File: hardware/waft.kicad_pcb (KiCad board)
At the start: 2 copper layers, 58 x 109 mm, 57 parts, among them IC1 VL6180x_Composite, J1 CONN_01X02, J10 Conn_01x10_Female, J11 Conn_01x10_Male, J12 Conn_01x10_Male, J2 CONN_01X01, J3 Thonkiconn, J4 Conn_02x05_Odd_Even, J5 Thonkiconn, J6 Thonkiconn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

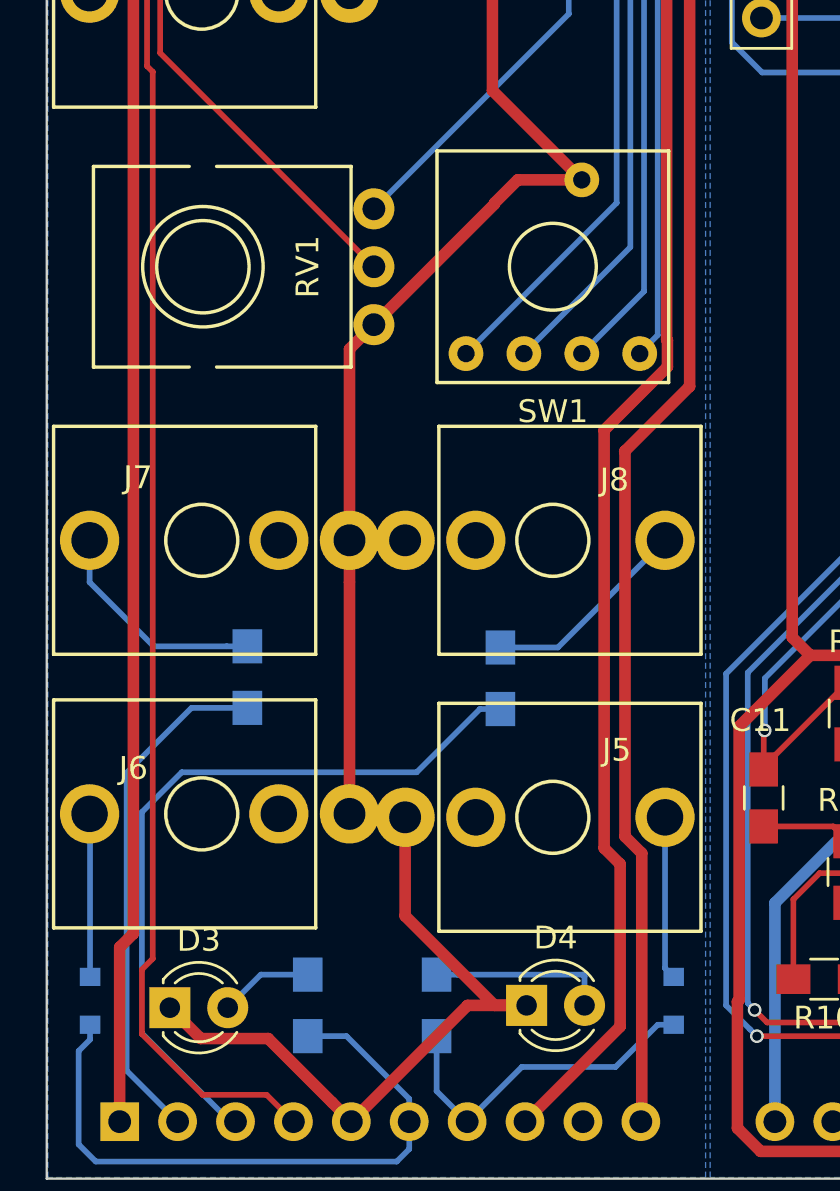
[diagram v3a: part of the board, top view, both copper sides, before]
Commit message: Started Front panel design
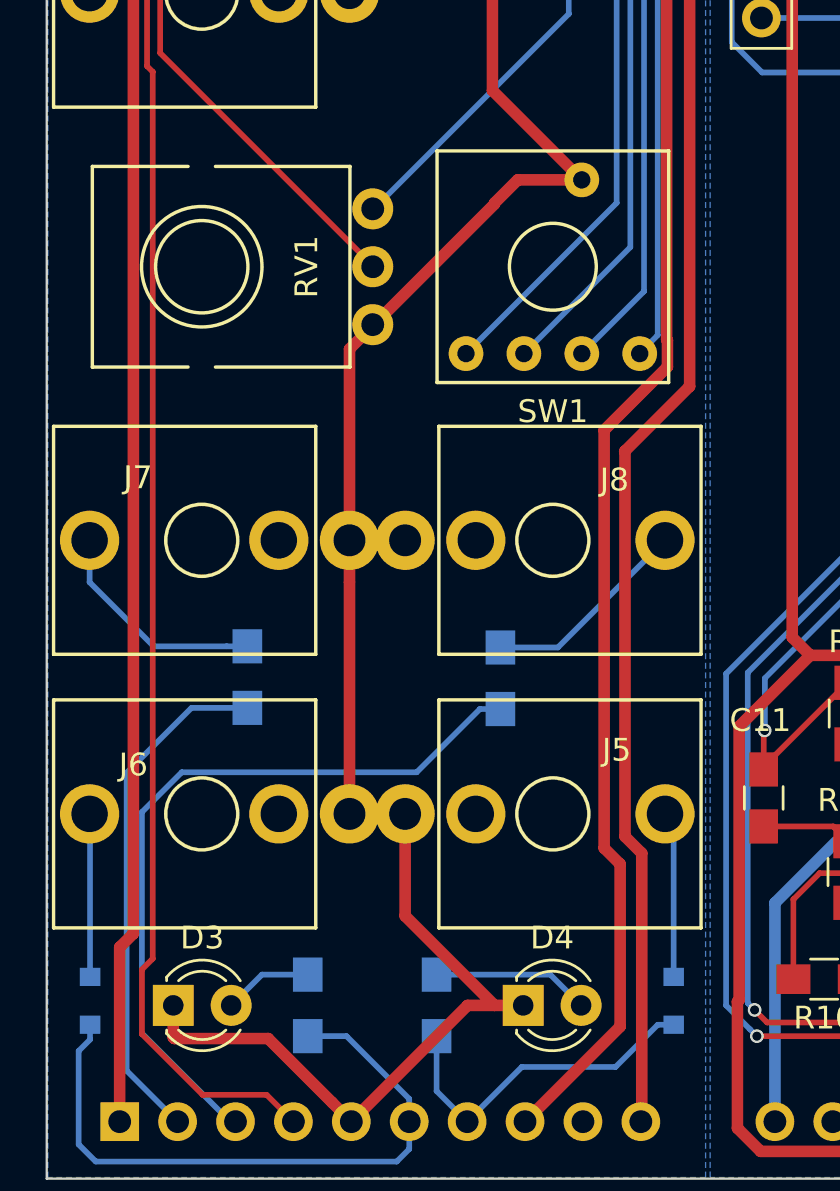
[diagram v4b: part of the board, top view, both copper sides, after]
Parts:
- moved D3 0.18 mm to (46.4, 152.8)
- moved J6 0.15 mm to (63.0, 144.4)
- moved D4 0.15 mm to (61.8, 152.8)
- moved RV1 0.05 mm to (47.6, 120.4)
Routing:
- net Net-(D4-Pad2): track 7.79 -> 6.90 mm
- net GND: track 446.9 -> 446.1 mm
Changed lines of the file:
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@@
   (general
     (links 148)
-    (no_connects 148)
-    (area 40.799999 51.349999 98.900001 160.450001)
+    (no_connects 5)
+    (area 39.015 46.104761 100.535 165.695239)
     (thickness 1.6)
     (drawings 12)
-    (tracks 651)
+    (tracks 649)
     (zones 0)
     (modules 57)
@@
   )
   (module LEDs:LED_D3.0mm (layer F.Cu)
-    (at 46.25 152.9)
+    (at 46.4 152.8)
     (descr "LED, diameter 3.0mm, 2 pins")
     (tags "LED diameter 3.0mm 2 pins")
@@
   )
   (module LEDs:LED_D3.0mm (layer F.Cu)
-    (at 61.9 152.8)
+    (at 61.75 152.8)
     (descr "LED, diameter 3.0mm, 2 pins")
     (tags "LED diameter 3.0mm 2 pins")
@@
   )
   (module europi:Thonkiconn (layer F.Cu)
-    (at 63.05 144.55 270)
+    (at 63.05 144.4 270)
     (fp_text reference J6 (at -2.15 18.4 360) (layer F.SilkS)
       (effects (font (size 1 1) (thickness 0.15)))
@@
   )
   (module europi:Alpha_9mm_Vertical (layer F.Cu)
-    (at 47.7 120.4 90)
+    (at 47.65 120.4 90)
     (fp_text reference RV1 (at 0 4.6 90) (layer F.SilkS)
       (effects (font (size 1 1) (thickness 0.15)))
@@
   (segment (start 73.05 53.9) (end 73.05 55.258) (width 0.508) (layer F.Cu) (net 1))
   (segment (start 73.05 55.258) (end 71.65 56.658) (width 0.508) (layer F.Cu) (net 1))
+  (segment (start 46.4 152.8) (end 46.4 154.208) (width 0.508) (layer F.Cu) (net 2))
+  (segment (start 46.4 154.208) (end 46.446001 154.254001) (width 0.508) (layer F.Cu) (net 2))
+  (segment (start 46.446001 154.254001) (end 50.564001 154.254001) (width 0.508) (layer F.Cu) (net 2))
+  (segment (start 50.564001 154.254001) (end 53.360001 157.050001) (width 0.508) (layer F.Cu) (net 2))
+  (segment (start 53.360001 157.050001) (end 54.21 157.9) (width 0.508) (layer F.Cu) (net 2))
+  (segment (start 60.492 152.8) (end 59.31 152.8) (width 0.508) (layer F.Cu) (net 2))
+  (segment (start 61.75 152.8) (end 60.492 152.8) (width 0.508) (layer F.Cu) (net 2))
+  (segment (start 56.57 148.878) (end 56.57 144.4) (width 0.508) (layer F.Cu) (net 2))
+  (segment (start 54.13 144.4) (end 56.57 144.4) (width 0.508) (layer F.Cu) (net 2))
   (segment (start 85.75 53.9) (end 85.75 57) (width 0.508) (layer F.Cu) (net 2))
   (segment (start 85.75 57) (end 86.59 57.84) (width 0.508) (layer F.Cu) (net 2))
@@
   (segment (start 78.53 96.64) (end 83.61 91.56) (width 0.508) (layer B.Cu) (net 2))
   (segment (start 83.61 91.56) (end 93.77 91.56) (width 0.508) (layer B.Cu) (net 2))
-  (segment (start 46.25 152.9) (end 47.604001 154.254001) (width 0.508) (layer F.Cu) (net 2))
-  (segment (start 47.604001 154.254001) (end 50.564001 154.254001) (width 0.508) (layer F.Cu) (net 2))
-  (segment (start 50.564001 154.254001) (end 53.360001 157.050001) (width 0.508) (layer F.Cu) (net 2))
-  (segment (start 53.360001 157.050001) (end 54.21 157.9) (width 0.508) (layer F.Cu) (net 2))
   (segment (start 54.21 157.9) (end 59.31 152.8) (width 0.508) (layer F.Cu) (net 2))
-  (segment (start 59.31 152.8) (end 61.9 152.8) (width 0.508) (layer F.Cu) (net 2))
-  (segment (start 56.57 144.55) (end 56.57 148.878) (width 0.508) (layer F.Cu) (net 2))
   (segment (start 56.57 148.878) (end 60.492 152.8) (width 0.508) (layer F.Cu) (net 2))
-  (segment (start 60.492 152.8) (end 61.9 152.8) (width 0.508) (layer F.Cu) (net 2))
-  (segment (start 54.13 144.4) (end 56.42 144.4) (width 0.508) (layer F.Cu) (net 2))
-  (segment (start 56.42 144.4) (end 56.57 144.55) (width 0.508) (layer F.Cu) (net 2))
   (segment (start 54.13 132.4) (end 54.13 134.238477) (width 0.508) (layer F.Cu) (net 2))
   (segment (start 54.13 134.238477) (end 54.13 144.4) (width 0.508) (layer F.Cu) (net 2))
@@
   (segment (start 97.05 67.392) (end 97.05 69) (width 0.508) (layer B.Cu) (net 17))
   (segment (start 89.13 60.73) (end 89.13 63.27) (width 0.508) (layer F.Cu) (net 17))
-  (segment (start 48.79 152.9) (end 50.24 151.45) (width 0.25) (layer B.Cu) (net 18))
-  (segment (start 50.24 151.45) (end 52.3 151.45) (width 0.25) (layer B.Cu) (net 18))
-  (segment (start 64.44 152.8) (end 64.44 151.527208) (width 0.25) (layer B.Cu) (net 19))
-  (segment (start 64.44 151.527208) (end 64.362792 151.45) (width 0.25) (layer B.Cu) (net 19))
-  (segment (start 64.362792 151.45) (end 58.85 151.45) (width 0.25) (layer B.Cu) (net 19))
-  (segment (start 58.85 151.45) (end 57.95 151.45) (width 0.25) (layer B.Cu) (net 19))
+  (segment (start 48.94 152.8) (end 50.29 151.45) (width 0.25) (layer B.Cu) (net 18))
+  (segment (start 50.29 151.45) (end 52.3 151.45) (width 0.25) (layer B.Cu) (net 18))
+  (segment (start 57.95 151.45) (end 62.94 151.45) (width 0.25) (layer B.Cu) (net 19))
+  (segment (start 62.94 151.45) (end 64.29 152.8) (width 0.25) (layer B.Cu) (net 19))
   (segment (start 42.75 151.55) (end 42.75 144.42) (width 0.25) (layer B.Cu) (net 20))
   (segment (start 42.75 144.42) (end 42.73 144.4) (width 0.25) (layer B.Cu) (net 20))
-  (segment (start 67.97 144.55) (end 67.97 151.17) (width 0.25) (layer B.Cu) (net 21))
-  (segment (start 67.97 151.17) (end 68.35 151.55) (width 0.25) (layer B.Cu) (net 21))
+  (segment (start 68.35 151.55) (end 68.35 144.78) (width 0.25) (layer B.Cu) (net 21))
+  (segment (start 68.35 144.78) (end 67.97 144.4) (width 0.25) (layer B.Cu) (net 21))
   (segment (start 72.2 92.7) (end 72.2 99.1) (width 0.25) (layer F.Cu) (net 22))
   (segment (start 72.2 92.7) (end 72.2 86.5) (width 0.25) (layer F.Cu) (net 22))

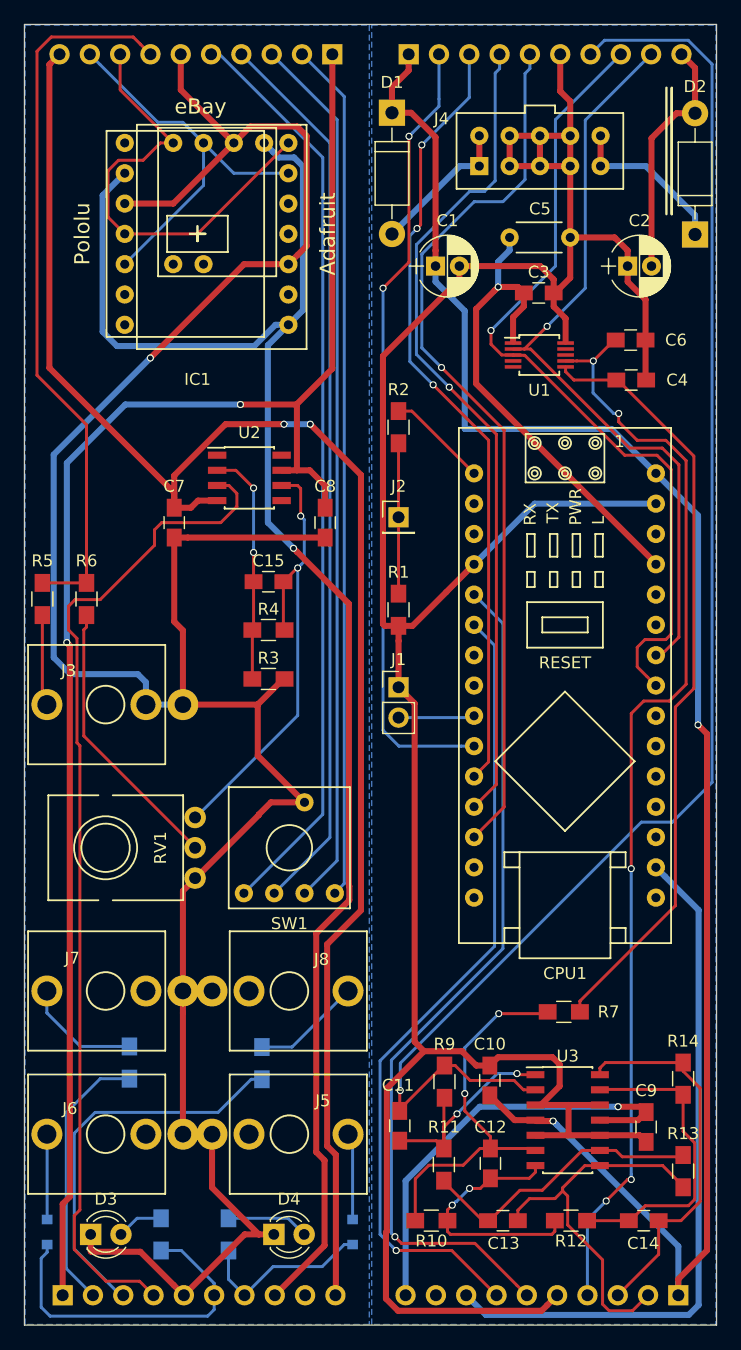
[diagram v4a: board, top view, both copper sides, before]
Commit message: Silk screen graphics
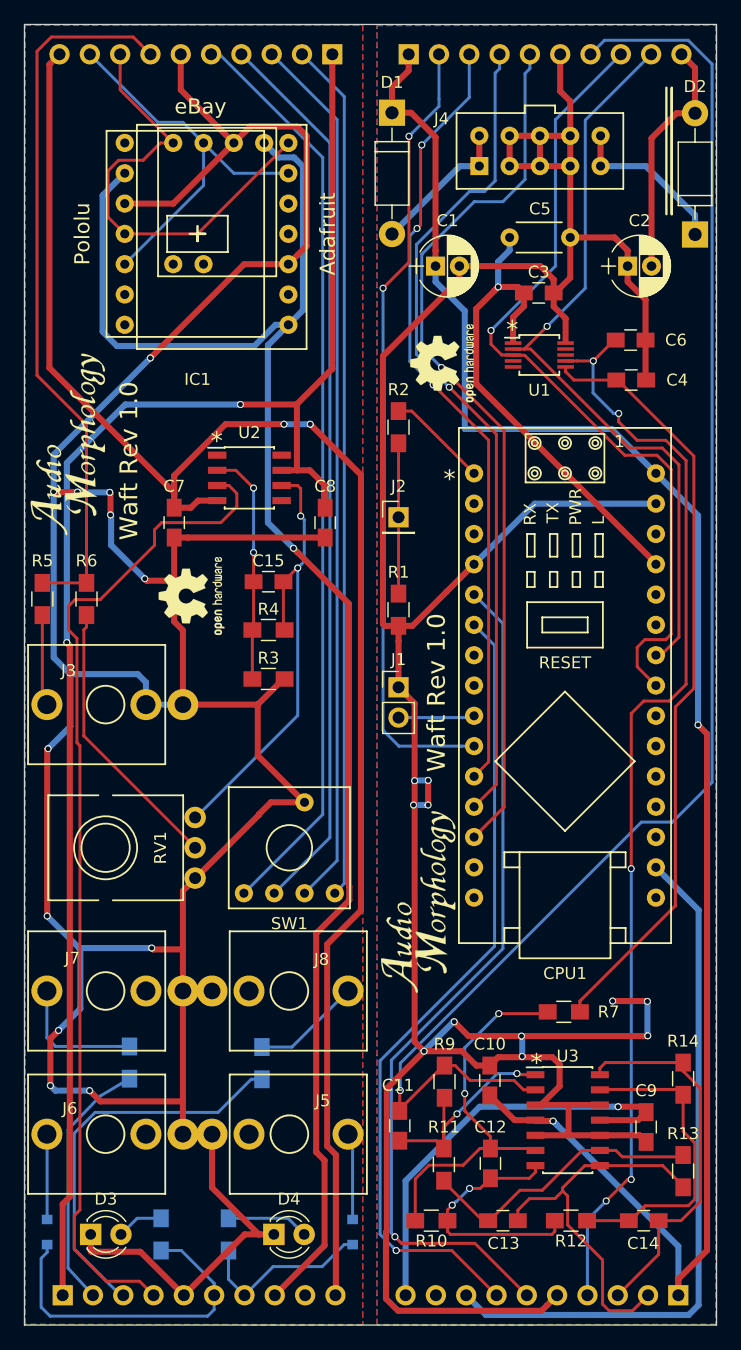
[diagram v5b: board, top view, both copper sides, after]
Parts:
- added ?: , europi:AM_Logo, F.Cu at (73.8, 125.0)
- added ?: , europi:AM_Logo, B.Cu at (86.6, 98.1)
- added ?: , europi:AM_Logo, F.Cu at (44.5, 86.6)
- added ?: , europi:AM_Logo, B.Cu at (53.3, 89.3)
- added REF***: OSHW-Logo2_7.3x6mm_SilkScreen, Symbols:OSHW-Logo2_7.3x6mm_SilkScreen, F.Cu at (54.9, 99.3)
- added REF***: OSHW-Logo2_7.3x6mm_SilkScreen, Symbols:OSHW-Logo2_7.3x6mm_SilkScreen, F.Cu at (75.9, 79.8)
- added REF***: OSHW-Logo2_7.3x6mm_SilkScreen, Symbols:OSHW-Logo2_7.3x6mm_SilkScreen, B.Cu at (88.1, 132.0)
- added REF***: OSHW-Logo2_7.3x6mm_SilkScreen, Symbols:OSHW-Logo2_7.3x6mm_SilkScreen, B.Cu at (53.4, 100.0)
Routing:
- net GND: track 446.1 -> 552.5 mm, vias 1 -> 23
- net CV1b: track 22.7 -> 21.4 mm
- net Net-(J7-Pad3): track 9.92 -> 11.1 mm
- added copper zone on F.Cu, net GND
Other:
- board text added: "*"
- board text added: "Waft Rev 1.0"

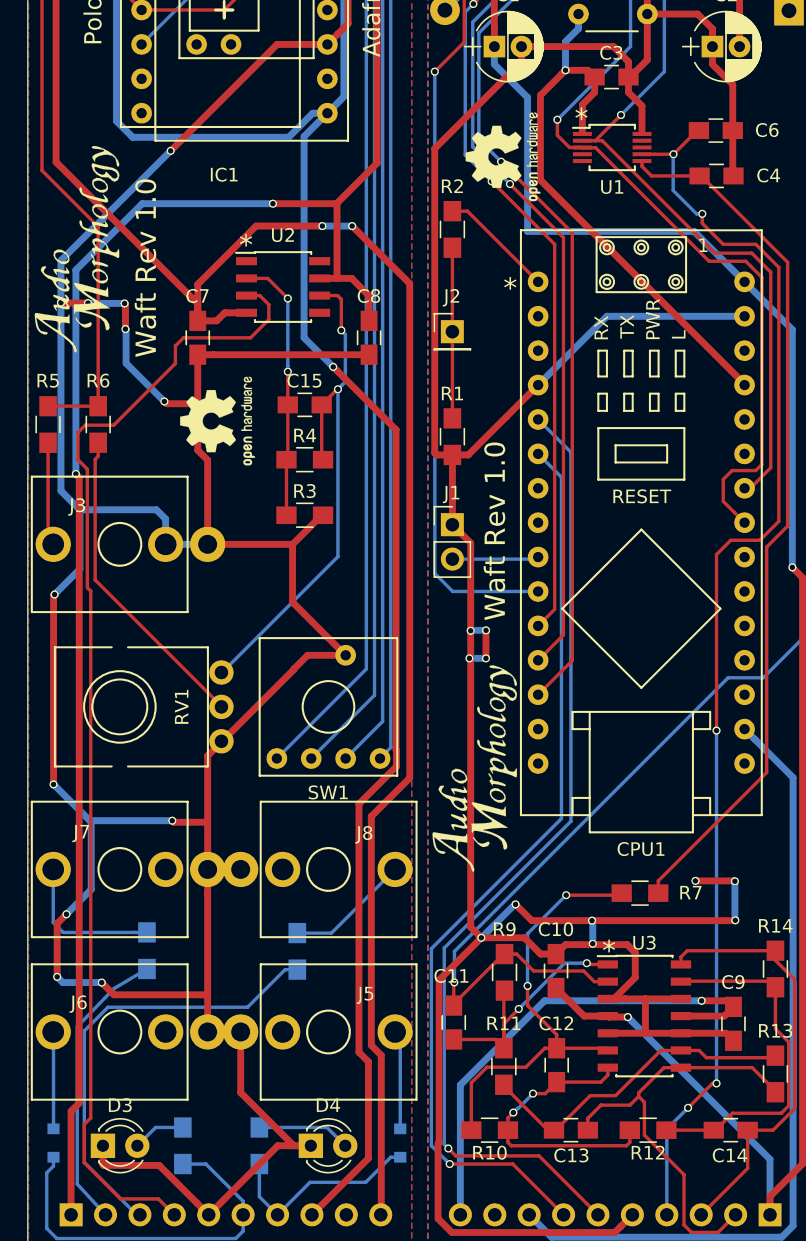
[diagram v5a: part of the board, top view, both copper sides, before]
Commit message: final cosmetic adjustments to Rev 1.0 Layout
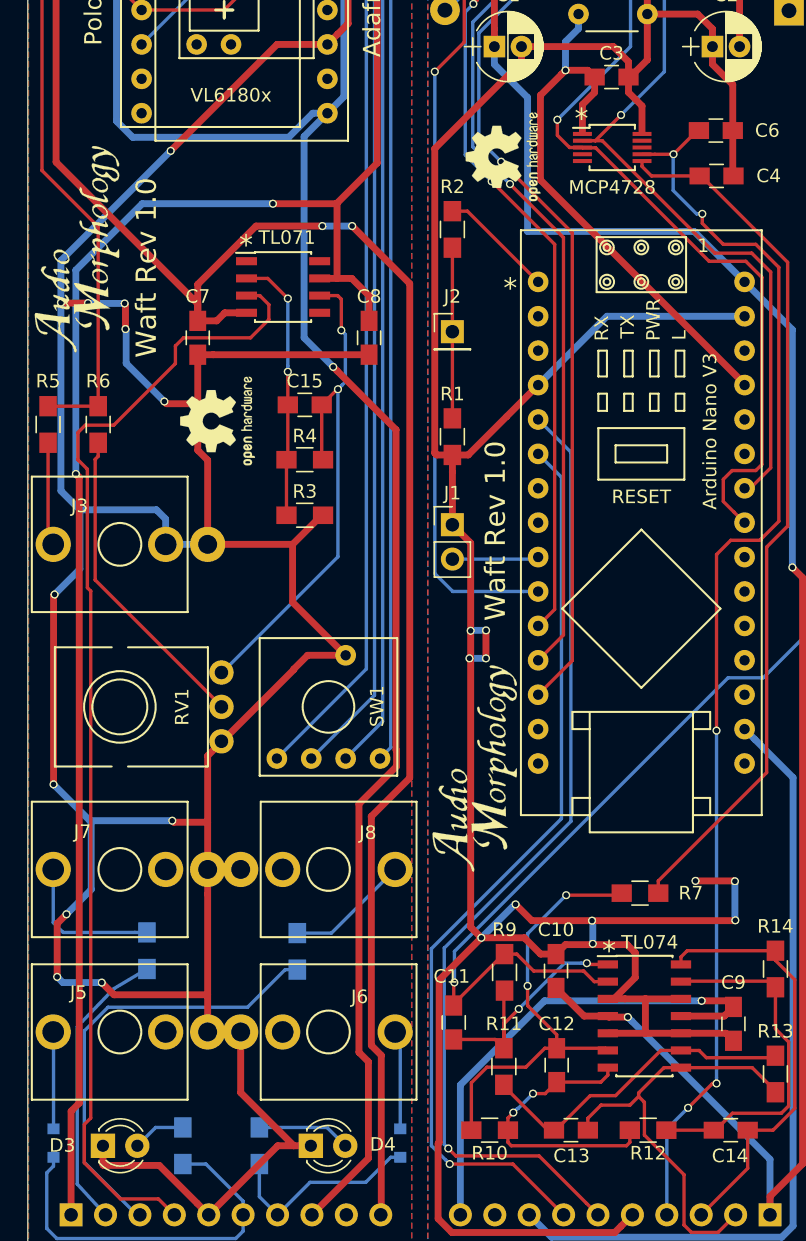
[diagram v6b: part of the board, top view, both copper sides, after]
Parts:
- Arduino Nano V3: renamed from CPU1
- renumbered U1 to MCP4728, U2 to TL071, U3 to TL074, IC1 to VL6180x
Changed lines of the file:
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@@
     (aux_axis_origin 0 0)
     (grid_origin 34.55 113.6)
-    (visible_elements 7FFFFF1F)
+    (visible_elements 7FFFFF3F)
     (pcbplotparams
       (layerselection 0x01430_80000001)
@@
   (module europi:Arduino_Nano_V3 (layer F.Cu)
     (at 86.15 106.8)
-    (fp_text reference CPU1 (at 0 24.13) (layer F.SilkS)
+    (fp_text reference "Arduino Nano V3" (at 5.0674 -6.7509 90) (layer F.SilkS)
       (effects (font (size 1 1) (thickness 0.15)))
     )
@@
     (descr "LED, diameter 3.0mm, 2 pins")
     (tags "LED diameter 3.0mm 2 pins")
-    (fp_text reference D3 (at 1.27 -2.96) (layer F.SilkS)
+    (fp_text reference D3 (at -2.9981 -0.0205) (layer F.SilkS)
       (effects (font (size 1 1) (thickness 0.15)))
     )
@@
     (descr "LED, diameter 3.0mm, 2 pins")
     (tags "LED diameter 3.0mm 2 pins")
-    (fp_text reference D4 (at 1.27 -2.96) (layer F.SilkS)
+    (fp_text reference D4 (at 5.312 -0.0967) (layer F.SilkS)
       (effects (font (size 1 1) (thickness 0.15)))
     )
@@
   (module europi:VL6180x_Composite (layer F.Cu)
     (at 55.35 68.95)
-    (fp_text reference IC1 (at 0 12.192) (layer F.SilkS)
+    (fp_text reference VL6180x (at 0.5106 6.296) (layer F.SilkS)
       (effects (font (size 1 1) (thickness 0.15)))
     )
@@
   (module europi:Thonkiconn (layer F.Cu)
     (at 47.65 108.4 90)
-    (fp_text reference J3 (at 2.85 -3.1 180) (layer F.SilkS)
+    (fp_text reference J3 (at 2.8391 -2.9781 180) (layer F.SilkS)
       (effects (font (size 1 1) (thickness 0.15)))
     )
@@
   (module europi:Thonkiconn (layer F.Cu)
     (at 47.65 144.4 90)
-    (fp_text reference J5 (at 2.8 18.2 180) (layer F.SilkS)
+    (fp_text reference J5 (at 2.9108 -3.0543 180) (layer F.SilkS)
       (effects (font (size 1 1) (thickness 0.15)))
     )
@@
   (module europi:Thonkiconn (layer F.Cu)
     (at 63.05 144.4 270)
-    (fp_text reference J6 (at -2.15 18.4 360) (layer F.SilkS)
+    (fp_text reference J6 (at -2.5933 -2.2975 360) (layer F.SilkS)
       (effects (font (size 1 1) (thickness 0.15)))
     )
@@
   (module europi:Thonkiconn (layer F.Cu)
     (at 47.65 132.4 90)
-    (fp_text reference J7 (at 2.75 -2.8 180) (layer F.SilkS)
+    (fp_text reference J7 (at 2.7853 -2.7622 180) (layer F.SilkS)
       (effects (font (size 1 1) (thickness 0.15)))
     )
@@
   (module europi:Thonkiconn (layer F.Cu)
     (at 63.05 132.4 270)
-    (fp_text reference J8 (at -2.65 -2.7 360) (layer F.SilkS)
+    (fp_text reference J8 (at -2.7091 -2.9071 360) (layer F.SilkS)
       (effects (font (size 1 1) (thickness 0.15)))
     )
@@
   (module europi:10_Way_Coded_Switch (layer F.Cu)
     (at 63.05 120.4)
-    (fp_text reference SW1 (at 0 6.35) (layer F.SilkS)
+    (fp_text reference SW1 (at 3.5929 -0.0563 90) (layer F.SilkS)
       (effects (font (size 1 1) (thickness 0.15)))
     )
@@
     (tags "SSOP 0.5")
     (attr smd)
-    (fp_text reference U1 (at 0 2.95) (layer F.SilkS)
+    (fp_text reference MCP4728 (at 0 2.95) (layer F.SilkS)
       (effects (font (size 1 1) (thickness 0.15)))
     )
@@
     (tags "SOIC 1.27")
     (attr smd)
-    (fp_text reference U2 (at 0 -3.8) (layer F.SilkS)
+    (fp_text reference TL071 (at 0.2881 -3.6511) (layer F.SilkS)
       (effects (font (size 1 1) (thickness 0.15)))
     )
@@
     (tags "SOIC 1.27")
     (attr smd)
-    (fp_text reference U3 (at 0 -5.375) (layer F.SilkS)
-      (effects (font (size 1 1) (thickness 0.15)))
-    )
+    (fp_text reference TL074 (at 0.3974 -5.4442) (layer F.SilkS)
+      (effects (font (size 1 1) (thickness 0.15)))
+    )
